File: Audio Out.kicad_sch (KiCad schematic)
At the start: 14 parts

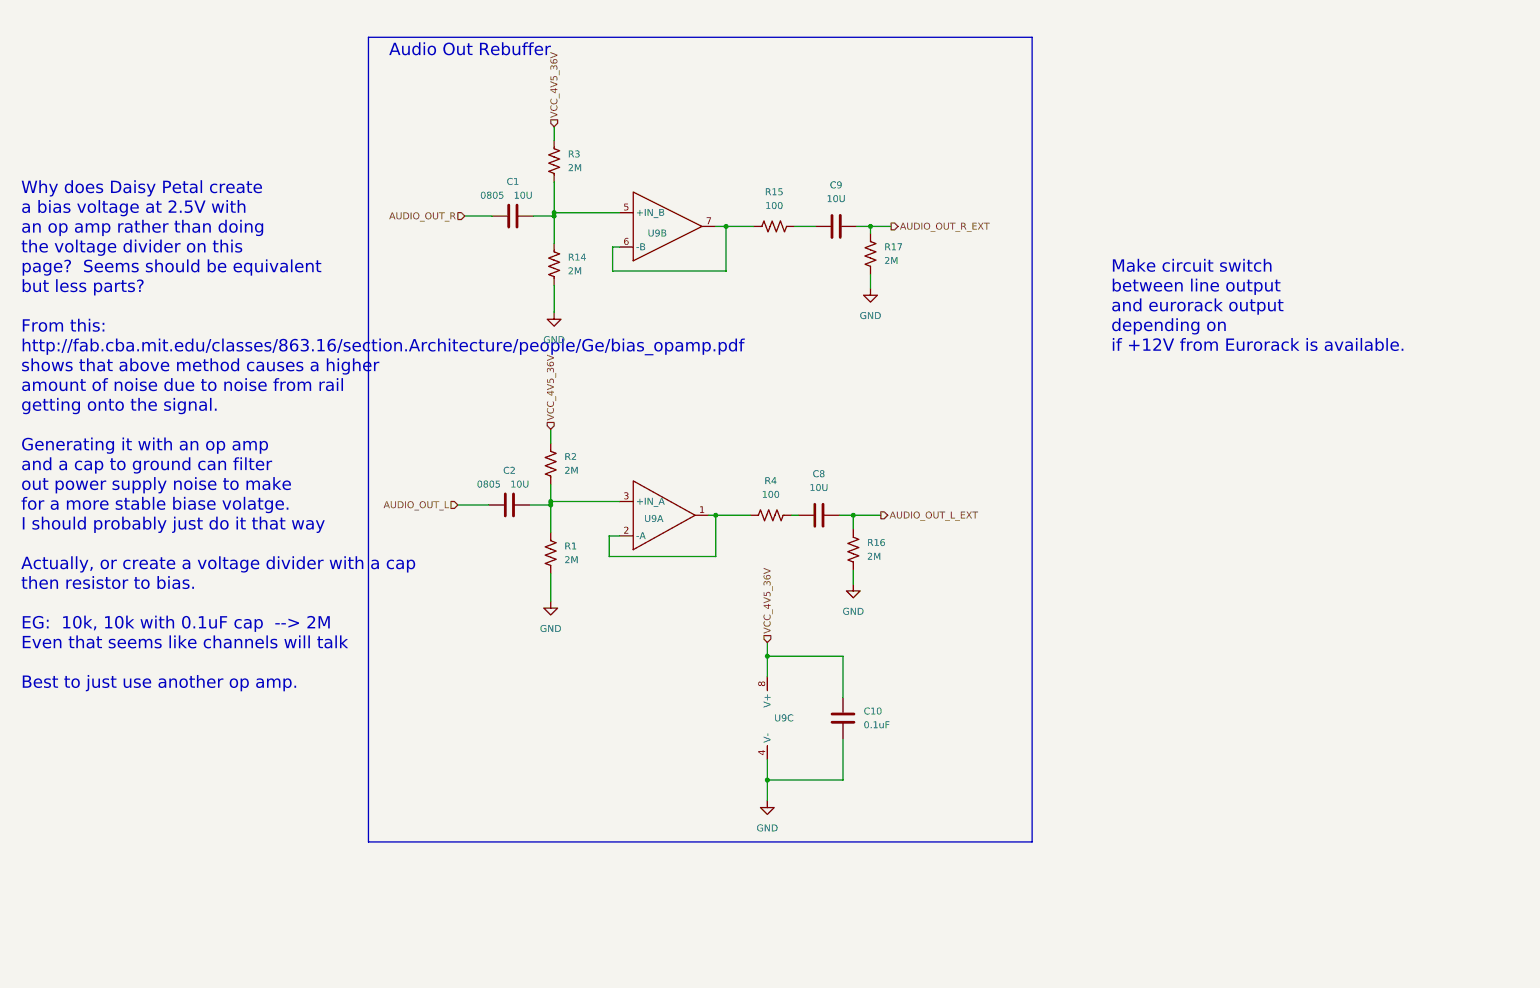
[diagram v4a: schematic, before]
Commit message: Update Audio out to switch between 1V ptp or 10V ptp based on jumper
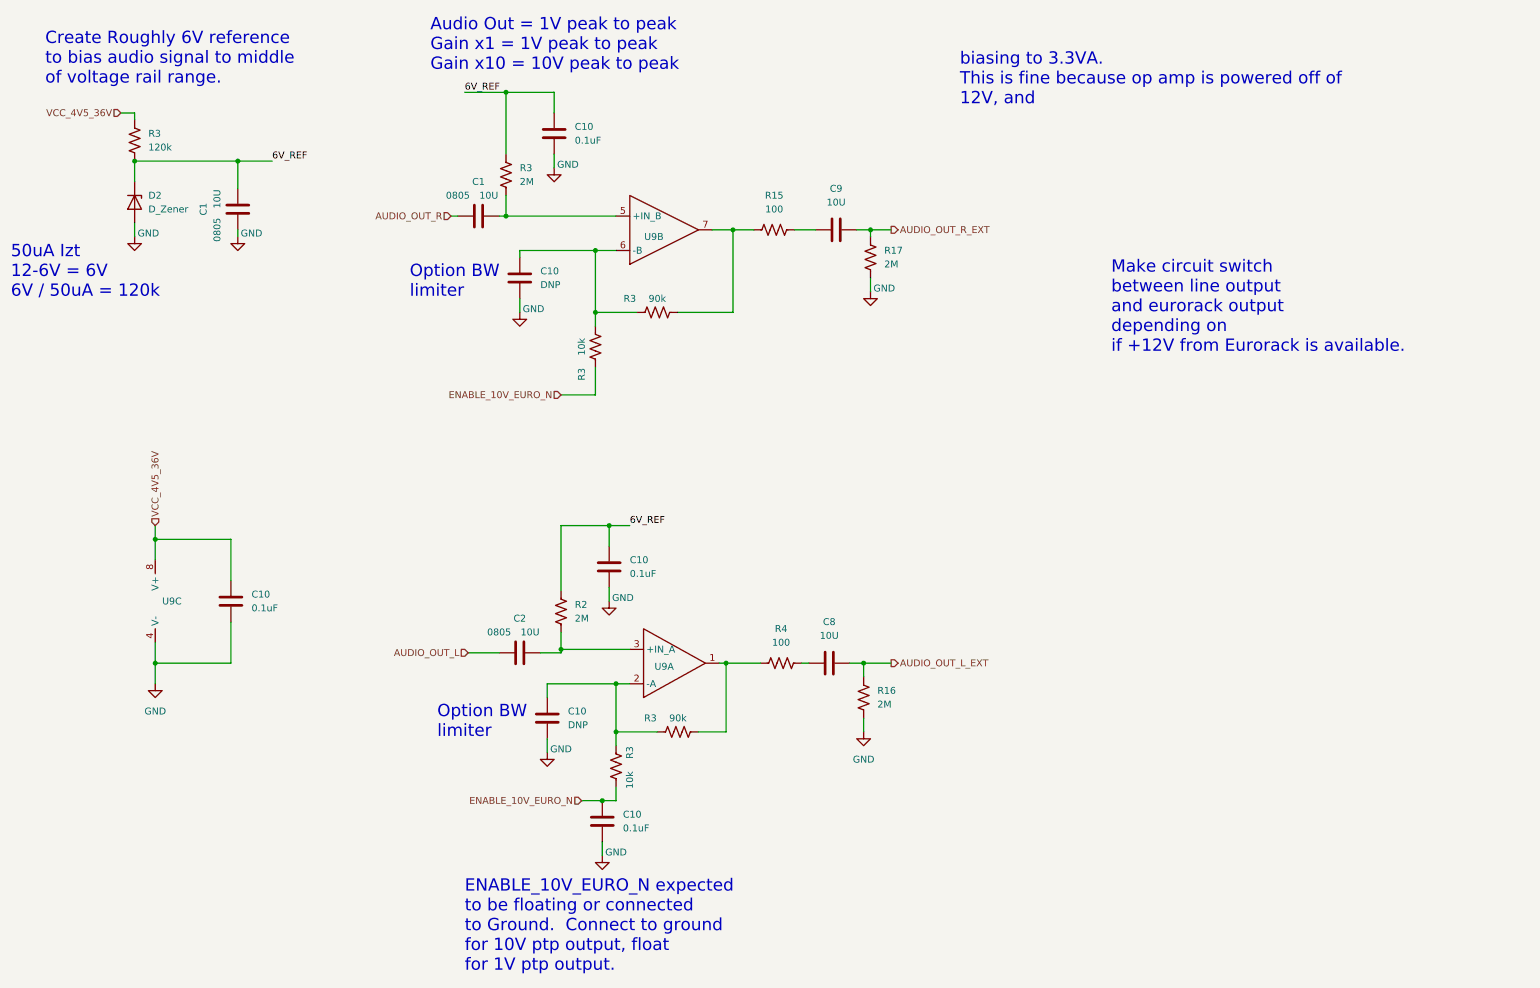
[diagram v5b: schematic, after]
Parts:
- removed R1, R14: 2M, Resistor_SMD:R_0402_1005Metric, symbol Device:R_US
- added C1: 10U, Capacitor_SMD:C_0805_2012Metric, symbol Device:C
- added C10 (x3): 0.1uF, Capacitor_SMD:C_0402_1005Metric, symbol Device:C
- added C10 (x2): DNP, Capacitor_SMD:C_0402_1005Metric, symbol Device:C
- added D2: D_Zener, symbol Device:D_Zener
- added R3 (x2): 10k, Resistor_SMD:R_0402_1005Metric, symbol Device:R_US
- added R3: 120k, Resistor_SMD:R_0402_1005Metric, symbol Device:R_US
- added R3 (x2): 90k, Resistor_SMD:R_0402_1005Metric, symbol Device:R_US
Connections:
- net GND: now also C1.1, C10.2, C10.2, C10.2, C10.2, C10.2, D2.2 (A)
- net VCC_4V5_36V: now also R3.1; no longer R2.1, R3.1
- net at R15.1, U9.7: now also R3.2; no longer U9.6 (-B)
- net at R4.1, U9.1: now also R3.2; no longer U9.2 (-A)
- new net: C10.1, R3.1, R3.2, U9.6 (-B)
- new net: C10.1, R3.1, R3.2, U9.2 (-A)
- new net 6V_REF: C1.2, C10.1, C10.1, D2.1 (K), R2.1, R3.1, R3.2
- new net ENABLE_10V_EURO_N: C10.1, R3.1, R3.1
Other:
- note added: "50uA Izt 12-6V = 6V 6V / 50uA = 120k"
- note added: "Audio Out = 1V peak to peak Gain x1 = 1V peak to peak Gain x10 = 10V peak to peak"
- note added: "Create Roughly 6V reference to bias audio signal to middle of voltage rail range."
- note added: "ENABLE_10V_EURO_N expected to be floating or connected to Ground. Connect to ground for 10V ptp output, float for 1V ptp output."
- note added: "Option BW limiter"
- note added: "biasing to 3.3VA. This is fine because op amp is powered off of 12V, and"
- note removed: "Audio Out Rebuffer"
- note removed: "Why does Daisy Petal create a bias voltage at 2.5V with an op amp rather than doing the voltage divider on this page? Seems should be equivalent but less parts? From this: http://fab.cba.mit.edu/classes/863.16/section.Architecture/people/Ge/bias_opamp.pdf shows that above method causes a higher amount of noise due to noise from rail getting onto the signal. Generating it with an op amp and a cap 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"
- moved on the sheet: C1, C10, C2, C8, C9, R15, R16, R17, R2, R3, R4, U9A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

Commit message: getting closer
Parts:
- removed C1: 10U, Capacitor_SMD:C_0805_2012Metric, symbol Device:C
- removed C10 (x3): 0.1uF, Capacitor_SMD:C_0402_1005Metric, symbol Device:C
- removed D2: D_Zener, symbol Device:D_Zener
- removed R3 (x2): 10k, Resistor_SMD:R_0402_1005Metric, symbol Device:R_US
- removed R3: 120k, Resistor_SMD:R_0402_1005Metric, symbol Device:R_US
- added R3 (x2): 2M, Resistor_SMD:R_0402_1005Metric, symbol Device:R_US
- R3: value 90k -> 0
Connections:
- net VCC_4V5_36V is gone; now on net VCC: C10.1, U9.8 (V+)
- net GND: now also R3.2, R3.2
- net at C1.2, R3.2, U9.5 (+IN_B): now also R3.1
- net at C2.2, R2.2, U9.3 (+IN_A): now also R3.1
- net 6V_REF renamed VCC
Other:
- note added: "Audio Out = 1V peak to peak Gain x1 = 1V peak to peak"
- note removed: "50uA Izt 12-6V = 6V 6V / 50uA = 120k"
- note removed: "Audio Out = 1V peak to peak Gain x1 = 1V peak to peak Gain x10 = 10V peak to peak"
- note removed: "Create Roughly 6V reference to bias audio signal to middle of voltage rail range."
- note removed: "ENABLE_10V_EURO_N expected to be floating or connected to Ground. Connect to ground for 10V ptp output, float for 1V ptp output."
- note removed: "Make circuit switch between line output and eurorack output depending on if +12V from Eurorack is available."
- note removed: "biasing to 3.3VA. This is fine because op amp is powered off of 12V, and"
- moved on the sheet: C10, C2, R2, U9C
